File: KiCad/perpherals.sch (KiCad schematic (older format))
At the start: 29 parts, among them J1 GPS, J10 LED, J2 DEPLOY, J3 TEMP, J4 ENV_SENSORS, J5 RF_DATA, J6 GND, J7 GND, J9 COMM_ANT, U1 Ai-Thinker-Ra-01, U2 DS18B20U+

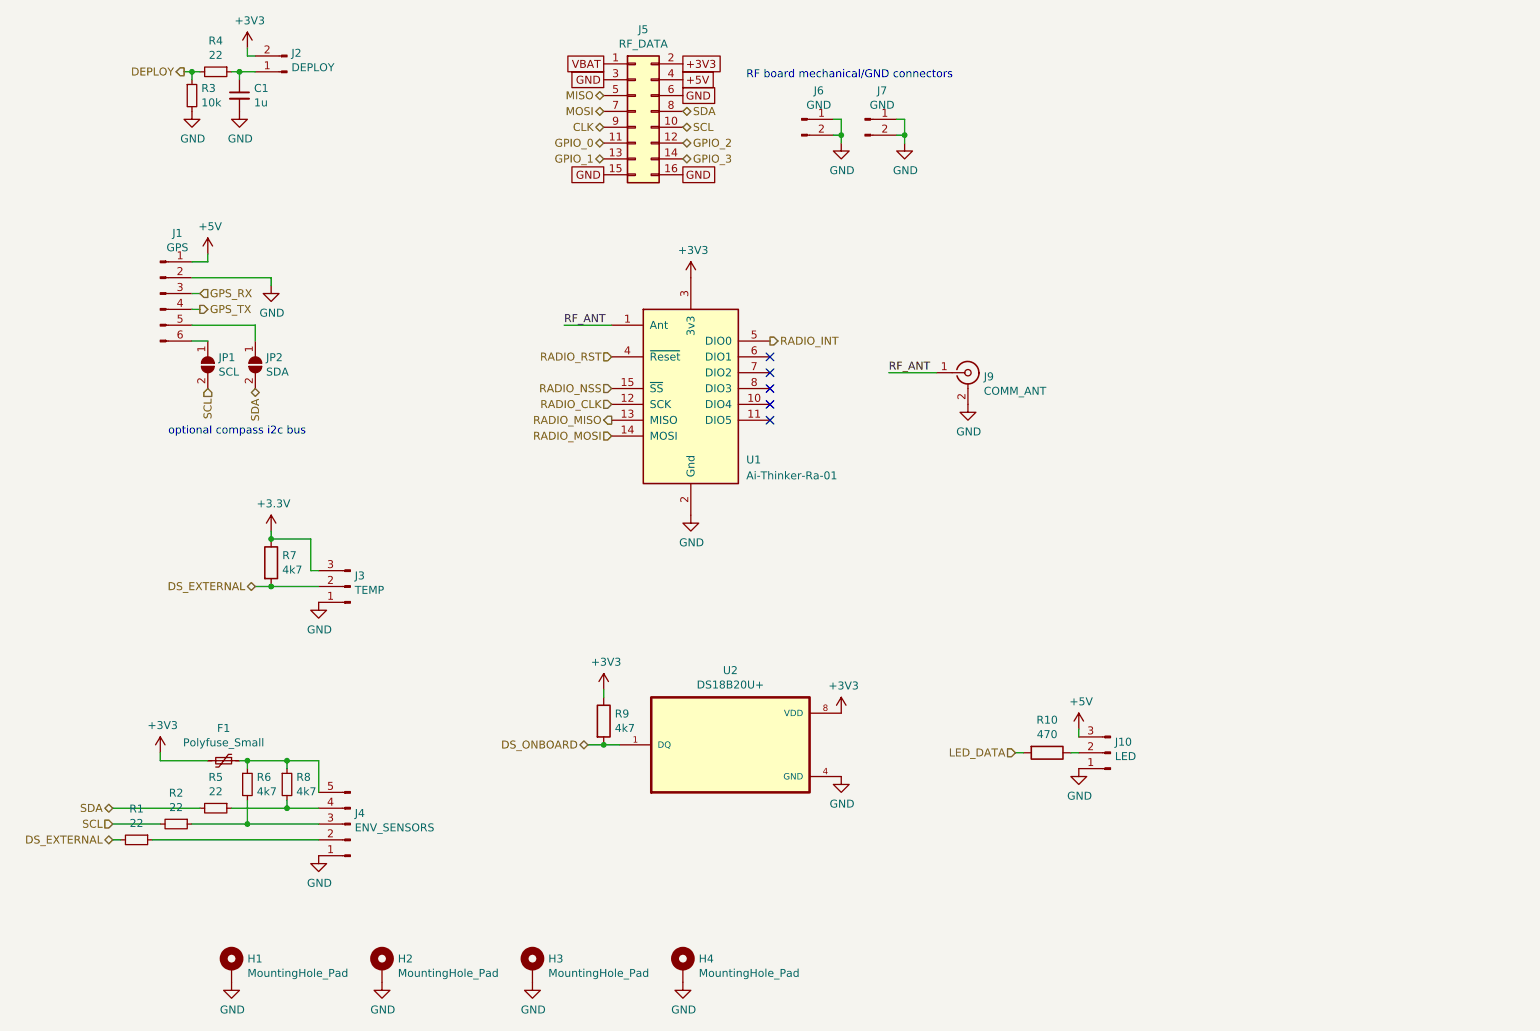
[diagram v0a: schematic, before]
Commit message: Added a button and a buzzer
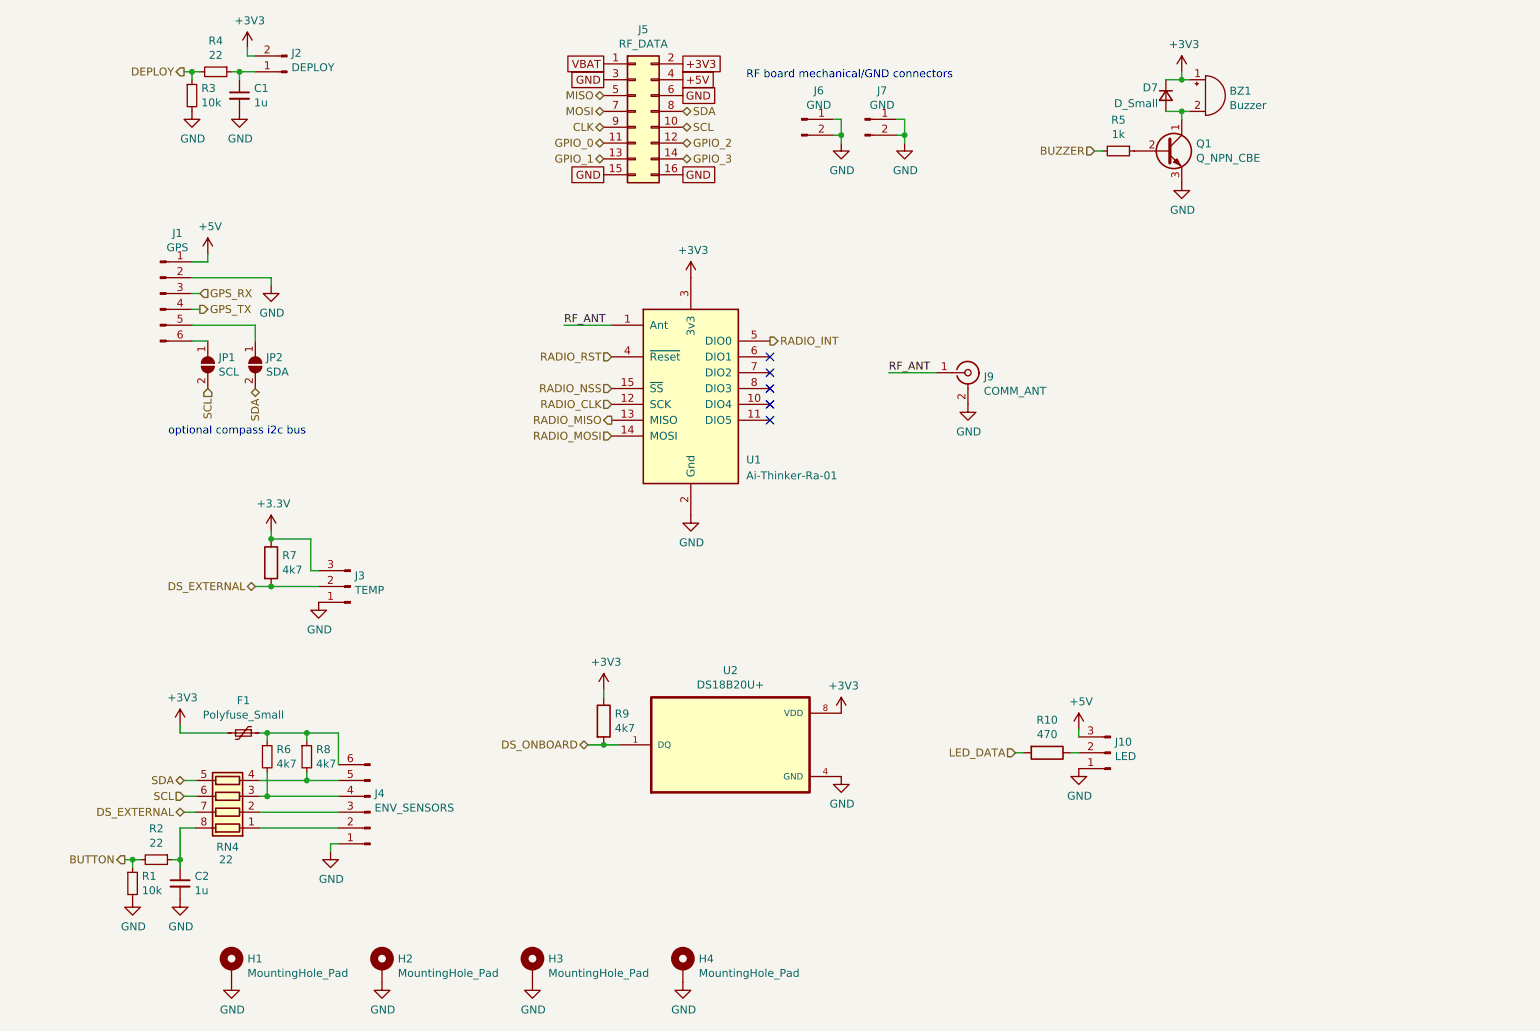
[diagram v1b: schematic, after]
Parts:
- removed J4: ENV_SENSORS, Connector_JST:JST_SHL_SM05B-SHLS-TF_1x05-1MP_P1.00mm_Horizontal, symbol Connector:Conn_01x05_Male
- added BZ1: Buzzer, Libs:MagneticBuzzer_INGHAi_GSC4417YA-16R4000, symbol Device:Buzzer
- added C2: 1u, Capacitor_SMD:C_0603_1608Metric_Pad1.05x0.95mm_HandSolder, symbol Device:C_Small
- added D7: D_Small, Diode_SMD:D_0603_1608Metric_Pad1.05x0.95mm_HandSolder, symbol Device:D_Small
- added J4: ENV_SENSORS, Connector_JST:JST_SH_BM06B-SRSS-TB_1x06-1MP_P1.00mm_Vertical, symbol Connector:Conn_01x06_Male
- added Q1: Q_NPN_CBE, Package_TO_SOT_SMD:SOT-23, symbol Device:Q_NPN_CBE
- added RN4: 22, Resistor_SMD:R_Array_Concave_4x0603, symbol Device:R_Pack04
- R1: value 22 -> 10k
- R5: value 22 -> 1k
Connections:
- net +3V3: now also BZ1.1 (-), D7.1 (K)
- net DS_EXTERNAL: now also RN4.7 (R2.2); no longer R1.2
- net GND: now also R1.2, C2.2, J4.1 (Pin_1), Q1.3 (E)
- net SCL: now also RN4.6 (R3.2); no longer R2.2
- net SDA: now also RN4.5 (R4.2); no longer R5.2
- net BUTTON: now reaches R1.1
- net BUTTON: now also R2.2
- net at R6.2: now also J4.4 (Pin_4), RN4.3 (R3.1); no longer R2.1
- net at R5.1: now also Q1.2 (B); no longer R8.2
- net at F1.1, R6.1, R8.1: now also J4.6 (Pin_6)
- new net: BZ1.2 (+), D7.2 (A), Q1.1 (C)
- new net: J4.2 (Pin_2), RN4.1 (R1.1)
- new net: J4.3 (Pin_3), RN4.2 (R2.1)
- new net: J4.5 (Pin_5), R8.2, RN4.4 (R4.1)
- new net: C2.1, R2.1, RN4.8 (R1.2)
- new net BUZZER: R5.2
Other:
- moved on the sheet: F1, R6, R8

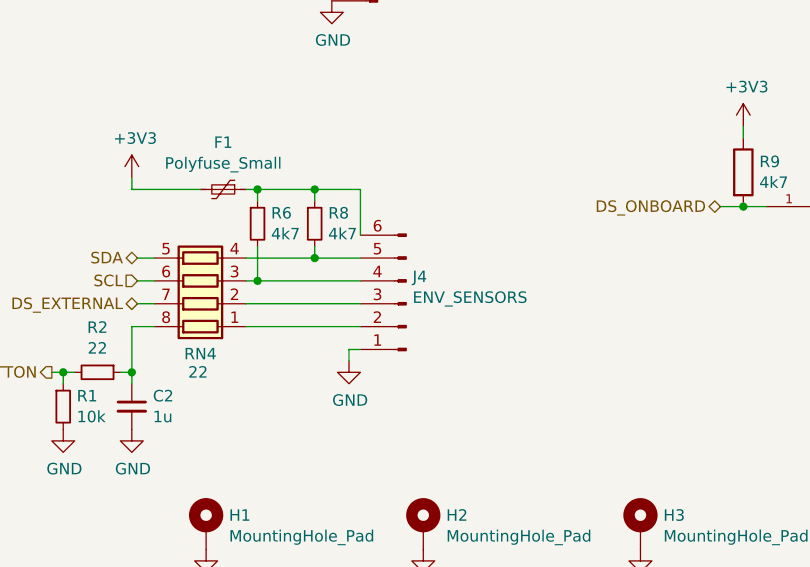
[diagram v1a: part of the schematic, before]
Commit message: Change all SH connectors to horizontal
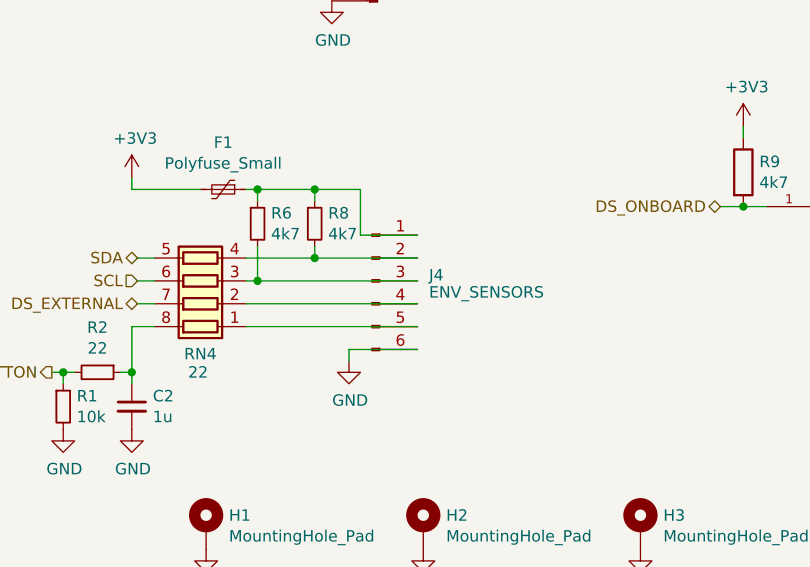
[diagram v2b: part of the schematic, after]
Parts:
- J1: footprint Connector_JST:JST_SHL_SM06B-SHLS-TF_1x06-1MP_P1.00mm_Horizontal -> Connector_JST:JST_SH_SM06B-SRSS-TB_1x06-1MP_P1.00mm_Horizontal
- J2: footprint Connector_JST:JST_SH_BM02B-SRSS-TB_1x02-1MP_P1.00mm_Vertical -> Connector_JST:JST_SH_SM02B-SRSS-TB_1x02-1MP_P1.00mm_Horizontal
- J3: footprint Connector_JST:JST_SH_BM03B-SRSS-TB_1x03-1MP_P1.00mm_Vertical -> Connector_JST:JST_SH_SM03B-SRSS-TB_1x03-1MP_P1.00mm_Horizontal
- J4: footprint Connector_JST:JST_SH_BM06B-SRSS-TB_1x06-1MP_P1.00mm_Vertical -> Connector_JST:JST_SH_SM06B-SRSS-TB_1x06-1MP_P1.00mm_Horizontal
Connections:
- net GND: now also J4.6 (Pin_6); no longer J4.1 (Pin_1)
- net at F1.1, R6.1, R8.1: now also J4.1 (Pin_1); no longer J4.6 (Pin_6)
- net at J4.2 (Pin_2): now also R8.2, RN4.4 (R4.1); no longer RN4.1 (R1.1)
- net at J4.3 (Pin_3): now also R6.2, RN4.3 (R3.1); no longer RN4.2 (R2.1)
- new net: J4.4 (Pin_4), RN4.2 (R2.1)
- new net: J4.5 (Pin_5), RN4.1 (R1.1)
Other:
- moved on the sheet: J4
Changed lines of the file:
@@
 F 0 "J2" H 2422 1082 50  0000 R CNN
 F 1 "DEPLOY" H 2422 1173 50  0000 R CNN
-F 2 "Connector_JST:JST_SH_BM02B-SRSS-TB_1x02-1MP_P1.00mm_Vertical" H 2450 1200 50  0001 C CNN
+F 2 "Connector_JST:JST_SH_SM02B-SRSS-TB_1x02-1MP_P1.00mm_Horizontal" H 2450 1200 50  0001 C CNN
 F 3 "~" H 2450 1200 50  0001 C CNN
 	1    2450 1200
@@
 F 0 "J3" H 2822 4382 50  0000 R CNN
 F 1 "TEMP" H 2822 4473 50  0000 R CNN
-F 2 "Connector_JST:JST_SH_BM03B-SRSS-TB_1x03-1MP_P1.00mm_Vertical" H 2850 4450 50  0001 C CNN
+F 2 "Connector_JST:JST_SH_SM03B-SRSS-TB_1x03-1MP_P1.00mm_Horizontal" H 2850 4450 50  0001 C CNN
 F 3 "~" H 2850 4450 50  0001 C CNN
 	1    2850 4450
@@
 F 0 "J1" H 1758 2981 50  0000 C CNN
 F 1 "GPS" H 1758 2890 50  0000 C CNN
-F 2 "Connector_JST:JST_SHL_SM06B-SHLS-TF_1x06-1MP_P1.00mm_Horizontal" H 1650 2600 50  0001 C CNN
+F 2 "Connector_JST:JST_SH_SM06B-SRSS-TB_1x06-1MP_P1.00mm_Horizontal" H 1650 2600 50  0001 C CNN
 F 3 "~" H 1650 2600 50  0001 C CNN
 	1    1650 2600
@@
 	1    0    0    -1
 $EndComp
-Wire Wire Line
-	2575 5675 2775 5675
-Wire Wire Line
-	2325 5775 2775 5775
 $Comp
 L power:GND #PWR0115
@@
 L Connector:Conn_01x06_Male J4
 U 1 1 5FD55774
-P 2975 5875
-F 0 "J4" H 2947 5757 50  0000 R CNN
-F 1 "ENV_SENSORS" H 2947 5848 50  0000 R CNN
-F 2 "Connector_JST:JST_SH_BM06B-SRSS-TB_1x06-1MP_P1.00mm_Vertical" H 2975 5875 50  0001 C CNN
-F 3 "~" H 2975 5875 50  0001 C CNN
-	1    2975 5875
-	-1   0    0    1
+P 2825 5775
+F 0 "J4" H 3075 5800 50  0000 L CNN
+F 1 "ENV_SENSORS" H 3075 5725 50  0000 L CNN
+F 2 "Connector_JST:JST_SH_SM06B-SRSS-TB_1x06-1MP_P1.00mm_Horizontal" H 2825 5775 50  0001 C CNN
+F 3 "~" H 2825 5775 50  0001 C CNN
+	1    2825 5775
+	1    0    0    -1
 $EndComp
 Wire Wire Line
 	2725 6125 2725 6075
 Wire Wire Line
-	2725 6075 2775 6075
-Wire Wire Line
 	2275 5675 2575 5675
 Wire Wire Line
 	2275 5775 2325 5775
-Wire Wire Line
-	2275 5875 2775 5875
 $Comp
 L Device:R_Pack04 RN?
@@
 $EndComp
 Wire Wire Line
-	2775 5975 2275 5975
-Wire Wire Line
 	1800 5675 1875 5675
 Wire Wire Line
@@
 	1775 5975 1875 5975
 Connection ~ 1775 6175
+Wire Wire Line
+	3025 5575 2775 5575
+Wire Wire Line
+	2575 5675 3025 5675
+Wire Wire Line
+	2325 5775 3025 5775
+Wire Wire Line
+	2275 5875 3025 5875
+Wire Wire Line
+	2275 5975 3025 5975
+Wire Wire Line
+	2725 6075 3025 6075
 $EndSCHEMATC

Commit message: Dirty production PCBs commit
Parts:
- added C3, C4: 100n, Capacitor_SMD:C_0603_1608Metric_Pad1.05x0.95mm_HandSolder, symbol Device:C_Small
- added U7: MMA8451QR1, Libs:QFN50P300X300X100-16N, symbol MMA8451QR1:MMA8451QR1
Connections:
- net +3V3: now also C4.1, U7.1 (VDDIO), U7.14 (VDD)
- net GND: now also C3.2, C4.2, U7.10 (GND_2), U7.12 (GND), U7.5 (GND_3), U7.7 (SA0)
- net SCL: now also U7.6 (SDA)
- net SDA: now also U7.4 (SCL)
- new net: C3.1, U7.2 (BYP)
- new net ACC_INT1: U7.11 (INT1)
- new net ACC_INT2: U7.9 (INT2)
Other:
- moved on the sheet: BZ1, D7, Q1, R5
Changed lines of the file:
@@
 L Device:Buzzer BZ1
 U 1 1 5FD39A54
-P 8250 1350
-F 0 "BZ1" H 8402 1379 50  0000 L CNN
-F 1 "Buzzer" H 8402 1288 50  0000 L CNN
-F 2 "Libs:MagneticBuzzer_INGHAi_GSC4417YA-16R4000" V 8225 1450 50  0001 C CNN
-F 3 "~" V 8225 1450 50  0001 C CNN
-	1    8250 1350
+P 9225 1400
+F 0 "BZ1" H 9377 1429 50  0000 L CNN
+F 1 "Buzzer" H 9377 1338 50  0000 L CNN
+F 2 "Libs:MagneticBuzzer_INGHAi_GSC4417YA-16R4000" V 9200 1500 50  0001 C CNN
+F 3 "~" V 9200 1500 50  0001 C CNN
+	1    9225 1400
 	1    0    0    -1
 $EndComp
@@
 L power:+3V3 #PWR04
 U 1 1 5FD39FD6
-P 8100 1200
-F 0 "#PWR04" H 8100 1050 50  0001 C CNN
-F 1 "+3V3" H 8115 1373 50  0000 C CNN
-F 2 "" H 8100 1200 50  0001 C CNN
-F 3 "" H 8100 1200 50  0001 C CNN
-	1    8100 1200
-	1    0    0    -1
-$EndComp
-Wire Wire Line
-	8100 1200 8100 1250
-Wire Wire Line
-	8100 1250 8150 1250
+P 9075 1250
+F 0 "#PWR04" H 9075 1100 50  0001 C CNN
+F 1 "+3V3" H 9090 1423 50  0000 C CNN
+F 2 "" H 9075 1250 50  0001 C CNN
+F 3 "" H 9075 1250 50  0001 C CNN
+	1    9075 1250
+	1    0    0    -1
+$EndComp
+Wire Wire Line
+	9075 1250 9075 1300
+Wire Wire Line
+	9075 1300 9125 1300
 $Comp
 L Device:Q_NPN_CBE Q1
 U 1 1 5FD3F00B
-P 8000 1700
-F 0 "Q1" H 8191 1746 50  0000 L CNN
-F 1 "Q_NPN_CBE" H 8191 1655 50  0000 L CNN
-F 2 "Package_TO_SOT_SMD:SOT-23" H 8200 1800 50  0001 C CNN
-F 3 "~" H 8000 1700 50  0001 C CNN
-	1    8000 1700
-	1    0    0    -1
-$EndComp
-Wire Wire Line
-	8100 1500 8100 1450
-Wire Wire Line
-	8100 1450 8150 1450
+P 8975 1750
+F 0 "Q1" H 9166 1796 50  0000 L CNN
+F 1 "Q_NPN_CBE" H 9166 1705 50  0000 L CNN
+F 2 "Package_TO_SOT_SMD:SOT-23" H 9175 1850 50  0001 C CNN
+F 3 "~" H 8975 1750 50  0001 C CNN
+	1    8975 1750
+	1    0    0    -1
+$EndComp
+Wire Wire Line
+	9075 1550 9075 1500
+Wire Wire Line
+	9075 1500 9125 1500
 $Comp
 L power:GND #PWR05
 U 1 1 5FD40E6E
-P 8100 1900
-F 0 "#PWR05" H 8100 1650 50  0001 C CNN
-F 1 "GND" H 8105 1727 50  0000 C CNN
-F 2 "" H 8100 1900 50  0001 C CNN
-F 3 "" H 8100 1900 50  0001 C CNN
-	1    8100 1900
+P 9075 1950
+F 0 "#PWR05" H 9075 1700 50  0001 C CNN
+F 1 "GND" H 9080 1777 50  0000 C CNN
+F 2 "" H 9075 1950 50  0001 C CNN
+F 3 "" H 9075 1950 50  0001 C CNN
+	1    9075 1950
 	1    0    0    -1
 $EndComp
@@
 L Device:R_Small R5
 U 1 1 5FD41C2C
-P 7700 1700
-F 0 "R5" V 7504 1700 50  0000 C CNN
-F 1 "1k" V 7595 1700 50  0000 C CNN
-F 2 "Resistor_SMD:R_0603_1608Metric_Pad1.05x0.95mm_HandSolder" H 7700 1700 50  0001 C CNN
-F 3 "~" H 7700 1700 50  0001 C CNN
-	1    7700 1700
+P 8675 1750
+F 0 "R5" V 8479 1750 50  0000 C CNN
+F 1 "1k" V 8570 1750 50  0000 C CNN
+F 2 "Resistor_SMD:R_0603_1608Metric_Pad1.05x0.95mm_HandSolder" H 8675 1750 50  0001 C CNN
+F 3 "~" H 8675 1750 50  0001 C CNN
+	1    8675 1750
 	0    1    1    0
 $EndComp
 Wire Wire Line
-	7550 1700 7600 1700
-Text HLabel 7550 1700 0    50   Input ~ 0
+	8525 1750 8575 1750
+Text HLabel 8525 1750 0    50   Input ~ 0
 BUZZER
 $Comp
 L Device:D_Small D7
 U 1 1 5FD441A9
-P 8000 1350
-F 0 "D7" V 7950 1300 50  0000 R CNN
-F 1 "D_Small" V 8050 1300 50  0000 R CNN
-F 2 "Diode_SMD:D_0603_1608Metric_Pad1.05x0.95mm_HandSolder" V 8000 1350 50  0001 C CNN
-F 3 "~" V 8000 1350 50  0001 C CNN
-	1    8000 1350
+P 8975 1400
+F 0 "D7" V 8925 1350 50  0000 R CNN
+F 1 "D_Small" V 9025 1350 50  0000 R CNN
+F 2 "Diode_SMD:D_0603_1608Metric_Pad1.05x0.95mm_HandSolder" V 8975 1400 50  0001 C CNN
+F 3 "~" V 8975 1400 50  0001 C CNN
+	1    8975 1400
 	0    1    1    0
 $EndComp
 Wire Wire Line
-	8100 1450 8000 1450
-Connection ~ 8100 1450
-Wire Wire Line
-	8000 1250 8100 1250
-Connection ~ 8100 1250
+	9075 1500 8975 1500
+Connection ~ 9075 1500
+Wire Wire Line
+	8975 1300 9075 1300
+Connection ~ 9075 1300
 $Comp
 L Connector:Conn_01x06_Male J4
@@
 Wire Wire Line
 	2725 6075 3025 6075
+$Comp
+L MMA8451QR1:MMA8451QR1 U7
+U 1 1 5FD9AB0B
+P 9100 3750
+F 0 "U7" H 9100 4820 50  0000 C CNN
+F 1 "MMA8451QR1" H 9100 4729 50  0000 C CNN
+F 2 "Libs:QFN50P300X300X100-16N" H 9100 3750 50  0001 L BNN
+F 3 "" H 9100 3750 50  0001 L BNN
+F 4 "84R7350" H 9100 3750 50  0001 L BNN "OC_NEWARK"
+F 5 "QFN-16" H 9100 3750 50  0001 L BNN "PACKAGE"
+F 6 "MMA8451QR1" H 9100 3750 50  0001 L BNN "MPN"
+F 7 "1908021" H 9100 3750 50  0001 L BNN "OC_FARNELL"
+F 8 "Freescale" H 9100 3750 50  0001 L BNN "SUPPLIER"
+	1    9100 3750
+	1    0    0    -1
+$EndComp
+Text HLabel 9800 3050 2    50   Output ~ 0
+ACC_INT1
+Text HLabel 9800 3150 2    50   Output ~ 0
+ACC_INT2
+$Comp
+L power:+3V3 #PWR07
+U 1 1 5FDA16E1
+P 8350 3000
+F 0 "#PWR07" H 8350 2850 50  0001 C CNN
+F 1 "+3V3" H 8365 3173 50  0000 C CNN
+F 2 "" H 8350 3000 50  0001 C CNN
+F 3 "" H 8350 3000 50  0001 C CNN
+	1    8350 3000
+	1    0    0    -1
+$EndComp
+Wire Wire Line
+	8350 3000 8350 3050
+Wire Wire Line
+	8350 3050 8400 3050
+Wire Wire Line
+	8350 3050 8350 3150
+Wire Wire Line
+	8350 3150 8400 3150
+Connection ~ 8350 3050
+Wire Wire Line
+	8400 4450 8350 4450
+Wire Wire Line
+	8350 4450 8350 4550
+Wire Wire Line
+	8350 4650 8400 4650
+Wire Wire Line
+	8350 4550 8400 4550
+Connection ~ 8350 4550
+Wire Wire Line
+	8350 4550 8350 4650
+$Comp
+L power:GND #PWR08
+U 1 1 5FDAE71D
+P 8350 4650
+F 0 "#PWR08" H 8350 4400 50  0001 C CNN
+F 1 "GND" H 8355 4477 50  0000 C CNN
+F 2 "" H 8350 4650 50  0001 C CNN
+F 3 "" H 8350 4650 50  0001 C CNN
+	1    8350 4650
+	1    0    0    -1
+$EndComp
+Text HLabel 8400 3550 0    50   BiDi ~ 0
+SCL
+Text HLabel 8400 3450 0    50   BiDi ~ 0
+SDA
+$Comp
+L power:GND #PWR06
+U 1 1 5FDC3B38
+P 7900 3600
+F 0 "#PWR06" H 7900 3350 50  0001 C CNN
+F 1 "GND" H 7905 3427 50  0000 C CNN
+F 2 "" H 7900 3600 50  0001 C CNN
+F 3 "" H 7900 3600 50  0001 C CNN
+	1    7900 3600
+	1    0    0    -1
+$EndComp
+$Comp
+L Device:C_Small C3
+U 1 1 5FDC5BAD
+P 7900 3500
+F 0 "C3" H 7992 3546 50  0000 L CNN
+F 1 "100n" H 7992 3455 50  0000 L CNN
+F 2 "Capacitor_SMD:C_0603_1608Metric_Pad1.05x0.95mm_HandSolder" H 7900 3500 50  0001 C CNN
+F 3 "~" H 7900 3500 50  0001 C CNN
+	1    7900 3500
+	1    0    0    -1
+$EndComp
+Wire Wire Line
+	8400 3350 7900 3350
+Wire Wire Line
+	7900 3350 7900 3400
+$Comp
+L power:GND #PWR010
+U 1 1 5FDCEE1C
+P 9950 4100
+F 0 "#PWR010" H 9950 3850 50  0001 C CNN
+F 1 "GND" H 9955 3927 50  0000 C CNN
+F 2 "" H 9950 4100 50  0001 C CNN
+F 3 "" H 9950 4100 50  0001 C CNN
+	1    9950 4100
+	1    0    0    -1
+$EndComp
+$Comp
+L Device:C_Small C4
+U 1 1 5FDCEE22
+P 9950 4000
+F 0 "C4" H 10042 4046 50  0000 L CNN
+F 1 "100n" H 10042 3955 50  0000 L CNN
+F 2 "Capacitor_SMD:C_0603_1608Metric_Pad1.05x0.95mm_HandSolder" H 9950 4000 50  0001 C CNN
+F 3 "~" H 9950 4000 50  0001 C CNN
+	1    9950 4000
+	1    0    0    -1
+$EndComp
+$Comp
+L power:+3V3 #PWR09
+U 1 1 5FDD247D
+P 9950 3900
+F 0 "#PWR09" H 9950 3750 50  0001 C CNN
+F 1 "+3V3" H 9965 4073 50  0000 C CNN
+F 2 "" H 9950 3900 50  0001 C CNN
+F 3 "" H 9950 3900 50  0001 C CNN
+	1    9950 3900
+	1    0    0    -1
+$EndComp
+Connection ~ 8350 4650
+$Comp
+L power:GND #PWR0125
+U 1 1 5FE11387
+P 8275 3700
+F 0 "#PWR0125" H 8275 3450 50  0001 C CNN
+F 1 "GND" H 8280 3527 50  0000 C CNN
+F 2 "" H 8275 3700 50  0001 C CNN
+F 3 "" H 8275 3700 50  0001 C CNN
+	1    8275 3700
+	1    0    0    -1
+$EndComp
+Wire Wire Line
+	8275 3700 8275 3650
+Wire Wire Line
+	8275 3650 8400 3650
 $EndSCHEMATC
